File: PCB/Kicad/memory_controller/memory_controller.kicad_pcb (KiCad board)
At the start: 6 copper layers, 0 parts

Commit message: pcb init
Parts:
- added C1: 100nF, Capacitor_SMD:C_0402_1005Metric, F.Cu at (262.9, 150.4)
- added C10: 100nF, Capacitor_SMD:C_0402_1005Metric, F.Cu at (259.7, 170.4)
- added C11: 100nF, Capacitor_SMD:C_0402_1005Metric, F.Cu at (243.1, 152.8)
- added C12: 100nF, Capacitor_SMD:C_0402_1005Metric, F.Cu at (243.1, 140.9)
- added C13: 100nF, Capacitor_SMD:C_0402_1005Metric, F.Cu at (213.7, 132.0)
- added C14: 100nF, Capacitor_SMD:C_0402_1005Metric, F.Cu at (196.7, 132.2)
- added C15: 100nF, Capacitor_SMD:C_0402_1005Metric, F.Cu at (174.9, 100.1)
- added C16: 100nF, Capacitor_SMD:C_0402_1005Metric, F.Cu at (174.6, 83.6)
- added C17: 100nF, Capacitor_SMD:C_0402_1005Metric, F.Cu at (219.2, 83.6)
- added C18: 100nF, Capacitor_SMD:C_0402_1005Metric, F.Cu at (218.9, 100.2)
- added C19: 100nF, Capacitor_SMD:C_0402_1005Metric, F.Cu at (235.8, 106.2)
- added C2: 100nF, Capacitor_SMD:C_0402_1005Metric, F.Cu at (263.0, 167.4)
- added C20: 100nF, Capacitor_SMD:C_0402_1005Metric, F.Cu at (235.8, 119.3)
- added C21: 100nF, Capacitor_SMD:C_0402_1005Metric, F.Cu at (259.9, 120.0)
- added C22: 100nF, Capacitor_SMD:C_0402_1005Metric, F.Cu at (259.9, 106.0)
- added C23: 100nF, Capacitor_SMD:C_0402_1005Metric, F.Cu at (160.3, 87.8)
- added C24: 100nF, Capacitor_SMD:C_0402_1005Metric, F.Cu at (160.4, 126.8)
- added C25: 100nF, Capacitor_SMD:C_0402_1005Metric, F.Cu at (212.4, 150.5)
- added C3: 100nF, Capacitor_SMD:C_0402_1005Metric, F.Cu at (162.9, 181.3)
- added C4: 100nF, Capacitor_SMD:C_0402_1005Metric, F.Cu at (162.7, 164.7)
- added C5: 100nF, Capacitor_SMD:C_0402_1005Metric, F.Cu at (193.7, 164.8)
- added C6: 100nF, Capacitor_SMD:C_0402_1005Metric, F.Cu at (193.5, 181.3)
- added C7: 100nF, Capacitor_SMD:C_0402_1005Metric, F.Cu at (241.6, 170.4)
- added C8: 100nF, Capacitor_SMD:C_0402_1005Metric, F.Cu at (241.6, 184.7)
- added C9: 100nF, Capacitor_SMD:C_0402_1005Metric, F.Cu at (259.7, 184.8)
- added H1: MountingHole_2.2mm_M2_DIN965_Pad, MountingHole:MountingHole_2.2mm_M2_DIN965_Pad, F.Cu at (281.4, 69.6)
- added H2: MountingHole_2.2mm_M2_DIN965_Pad, MountingHole:MountingHole_2.2mm_M2_DIN965_Pad, F.Cu at (281.0, 213.5)
- added H3: MountingHole_2.2mm_M2_DIN965_Pad, MountingHole:MountingHole_2.2mm_M2_DIN965_Pad, F.Cu at (87.5, 212.0)
- added H4: MountingHole_2.2mm_M2_DIN965_Pad, MountingHole:MountingHole_2.2mm_M2_DIN965_Pad, F.Cu at (87.4, 69.6)
- added U1: 74LS245, Package_SO:SOIC-20W_7.5x12.8mm_P1.27mm, F.Cu at (257.5, 142.0)
- added U10: 4b_fulladder__CD74HC283M96, mALUch_lib:CD_SOIC127P600X175-16N, F.Cu at (256.5, 191.9)
- added U11: 74LS377, Package_SO:SSOP-20_5.3x7.2mm_P0.65mm, F.Cu at (239.0, 146.8)
- added U12: 74LS377, Package_SO:SSOP-20_5.3x7.2mm_P0.65mm, F.Cu at (239.0, 158.8)
- added U13: 74LS245, Package_SO:SOIC-20W_7.5x12.8mm_P1.27mm, F.Cu at (205.2, 126.8)
- added U14: 74LS245, Package_SO:SOIC-20W_7.5x12.8mm_P1.27mm, F.Cu at (188.1, 126.9)
- added U15: 74LS245, Package_SO:SOIC-20W_7.5x12.8mm_P1.27mm, F.Cu at (180.2, 92.1)
- added U16: 74LS245, Package_SO:SOIC-20W_7.5x12.8mm_P1.27mm, F.Cu at (180.2, 108.3)
- added U17: 74LS245, Package_SO:SOIC-20W_7.5x12.8mm_P1.27mm, F.Cu at (213.8, 92.1)
- added U18: 74LS245, Package_SO:SOIC-20W_7.5x12.8mm_P1.27mm, F.Cu at (213.8, 108.3)
- added U19: 4xAND__SN74HC08DR, mALUch_lib:SOIC127P600X175-14N, F.Cu at (238.8, 112.8)
- added U2: 74LS245, Package_SO:SOIC-20W_7.5x12.8mm_P1.27mm, F.Cu at (257.5, 159.0)
- added U20: ~, mALUch_lib:SOIC127P600X175-14N, F.Cu at (238.8, 125.8)
- added U21: ~, mALUch_lib:SOIC127P600X175-14N, F.Cu at (257.0, 112.8)
- added U22: 4xAND__SN74HC08DR, mALUch_lib:SOIC127P600X175-14N, F.Cu at (257.0, 127.0)
- added U23: AT28C256-15PU, Package_DIP:DIP-28_W15.24mm_Socket, F.Cu at (141.6, 85.2)
- added U24: AT28C256-15PU, Package_DIP:DIP-28_W15.24mm_Socket, F.Cu at (141.6, 124.2)
- added U25: AS7C1026B-10TCN, Package_SO:TSOP-II-44_10.16x18.41mm_P0.8mm, F.Cu at (204.8, 150.5)
- added U3: 74LS245, Package_SO:SOIC-20W_7.5x12.8mm_P1.27mm, F.Cu at (168.2, 173.2)
- added U4: 74LS245, Package_SO:SOIC-20W_7.5x12.8mm_P1.27mm, F.Cu at (168.3, 189.4)
- added U5: 74LS245, Package_SO:SOIC-20W_7.5x12.8mm_P1.27mm, F.Cu at (188.2, 173.2)
- added U6: 74LS245, Package_SO:SOIC-20W_7.5x12.8mm_P1.27mm, F.Cu at (188.3, 189.4)
- added U7: 4b_fulladder__CD74HC283M96, mALUch_lib:CD_SOIC127P600X175-16N, F.Cu at (238.4, 177.5)
- added U8: 4b_fulladder__CD74HC283M96, mALUch_lib:CD_SOIC127P600X175-16N, F.Cu at (238.4, 191.9)
- added U9: 4b_fulladder__CD74HC283M96, mALUch_lib:CD_SOIC127P600X175-16N, F.Cu at (256.5, 177.5)
- added control1: ~, mALUch_lib:PinHeader_2x10_P2.54mm_Horizontal, F.Cu at (270.5, 116.6)
- added control2: ~, mALUch_lib:PinHeader_2x10_P2.54mm_Horizontal, F.Cu at (270.5, 145.1)
- added gpu1: ~, mALUch_lib:PinHeader_2x10_P2.54mm_Horizontal, F.Cu at (181.2, 203.0)
- added gpu2: ~, mALUch_lib:PinHeader_2x10_P2.54mm_Horizontal, F.Cu at (209.1, 203.0)
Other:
- board outline added: 203.5 x 150.8 mm

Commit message: LEDs + minor fixes
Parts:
- added Dd1: yellow, LED_SMD:LED_0603_1608Metric, F.Cu at (113.5, 92.5)
- added Dd10: yellow, LED_SMD:LED_0603_1608Metric, F.Cu at (114.2, 137.4)
- added Dd11: yellow, LED_SMD:LED_0603_1608Metric, F.Cu at (114.2, 143.0)
- added Dd12: yellow, LED_SMD:LED_0603_1608Metric, F.Cu at (114.2, 148.6)
- added Dd2: yellow, LED_SMD:LED_0603_1608Metric, F.Cu at (113.5, 98.1)
- added Dd3: yellow, LED_SMD:LED_0603_1608Metric, F.Cu at (113.3, 103.7)
- added Dd4: yellow, LED_SMD:LED_0603_1608Metric, F.Cu at (113.5, 109.3)
- added Dd5: yellow, LED_SMD:LED_0603_1608Metric, F.Cu at (113.5, 115.0)
- added Dd6: yellow, LED_SMD:LED_0603_1608Metric, F.Cu at (113.2, 120.6)
- added Dd7: yellow, LED_SMD:LED_0603_1608Metric, F.Cu at (113.5, 126.2)
- added Dd8: yellow, LED_SMD:LED_0603_1608Metric, F.Cu at (113.5, 131.8)
- added Dd9: yellow, LED_SMD:LED_0603_1608Metric, F.Cu at (114.0, 154.2)
- added Dpwr1: green, Diode_SMD:D_0603_1608Metric, F.Cu at (279.2, 181.2)
- added Dr0: red, LED_SMD:LED_0603_1608Metric, F.Cu at (97.8, 87.2)
- added Dr1: red, LED_SMD:LED_0603_1608Metric, F.Cu at (97.7, 92.5)
- added Dr10: red, LED_SMD:LED_0603_1608Metric, F.Cu at (98.4, 139.9)
- added Dr11: red, LED_SMD:LED_0603_1608Metric, F.Cu at (98.7, 145.2)
- added Dr12: red, LED_SMD:LED_0603_1608Metric, F.Cu at (98.5, 150.4)
- added Dr13: red, LED_SMD:LED_0603_1608Metric, F.Cu at (98.7, 155.7)
- added Dr14: red, LED_SMD:LED_0603_1608Metric, F.Cu at (98.7, 161.0)
- added Dr15: red, LED_SMD:LED_0603_1608Metric, F.Cu at (98.7, 166.2)
- added Dr2: red, LED_SMD:LED_0603_1608Metric, F.Cu at (97.7, 97.8)
- added Dr3: red, LED_SMD:LED_0603_1608Metric, F.Cu at (97.7, 103.0)
- added Dr4: red, LED_SMD:LED_0603_1608Metric, F.Cu at (97.8, 108.3)
- added Dr5: red, LED_SMD:LED_0603_1608Metric, F.Cu at (98.0, 113.6)
- added Dr6: red, LED_SMD:LED_0603_1608Metric, F.Cu at (98.0, 118.8)
- added Dr7: red, LED_SMD:LED_0603_1608Metric, F.Cu at (98.0, 124.1)
- added Dr8: red, LED_SMD:LED_0603_1608Metric, F.Cu at (98.0, 129.4)
- added Dr9: red, LED_SMD:LED_0603_1608Metric, F.Cu at (98.0, 134.6)
- added Rd1: 680, Resistor_SMD:R_0402_1005Metric, F.Cu at (110.0, 92.5)
- added Rd10: 680, Resistor_SMD:R_0402_1005Metric, F.Cu at (110.5, 137.4)
- added Rd11: 680, Resistor_SMD:R_0402_1005Metric, F.Cu at (110.5, 143.0)
- added Rd12: 680, Resistor_SMD:R_0402_1005Metric, F.Cu at (110.5, 148.6)
- added Rd2: 680, Resistor_SMD:R_0402_1005Metric, F.Cu at (110.0, 98.1)
- added Rd3: 680, Resistor_SMD:R_0402_1005Metric, F.Cu at (110.0, 103.7)
- added Rd4: 680, Resistor_SMD:R_0402_1005Metric, F.Cu at (110.0, 109.3)
- added Rd5: 680, Resistor_SMD:R_0402_1005Metric, F.Cu at (110.0, 115.0)
- added Rd6: 680, Resistor_SMD:R_0402_1005Metric, F.Cu at (110.0, 120.6)
- added Rd7: 680, Resistor_SMD:R_0402_1005Metric, F.Cu at (110.0, 126.2)
- added Rd8: 680, Resistor_SMD:R_0402_1005Metric, F.Cu at (110.0, 131.8)
- added Rd9: 680, Resistor_SMD:R_0402_1005Metric, F.Cu at (110.0, 154.2)
- added Rgp1: 680, Resistor_SMD:R_0402_1005Metric, F.Cu at (275.5, 181.2)
- added Rr0: 680, Resistor_SMD:R_0402_1005Metric, F.Cu at (94.5, 87.2)
- added Rr1: 680, Resistor_SMD:R_0402_1005Metric, F.Cu at (94.5, 92.5)
- added Rr10: 680, Resistor_SMD:R_0402_1005Metric, F.Cu at (95.0, 139.9)
- added Rr11: 680, Resistor_SMD:R_0402_1005Metric, F.Cu at (95.0, 145.2)
- added Rr12: 680, Resistor_SMD:R_0402_1005Metric, F.Cu at (95.0, 150.4)
- added Rr13: 680, Resistor_SMD:R_0402_1005Metric, F.Cu at (95.0, 155.7)
- added Rr14: 680, Resistor_SMD:R_0402_1005Metric, F.Cu at (95.0, 161.0)
- added Rr15: 680, Resistor_SMD:R_0402_1005Metric, F.Cu at (95.0, 166.2)
- added Rr2: 680, Resistor_SMD:R_0402_1005Metric, F.Cu at (94.5, 97.8)
- added Rr3: 680, Resistor_SMD:R_0402_1005Metric, F.Cu at (94.5, 103.0)
- added Rr4: 680, Resistor_SMD:R_0402_1005Metric, F.Cu at (94.5, 108.3)
- added Rr5: 680, Resistor_SMD:R_0402_1005Metric, F.Cu at (94.5, 113.6)
- added Rr6: 680, Resistor_SMD:R_0402_1005Metric, F.Cu at (94.5, 118.8)
- added Rr7: 680, Resistor_SMD:R_0402_1005Metric, F.Cu at (94.5, 124.1)
- added Rr8: 680, Resistor_SMD:R_0402_1005Metric, F.Cu at (94.5, 129.4)
- added Rr9: 680, Resistor_SMD:R_0402_1005Metric, F.Cu at (94.5, 134.6)
- H1, H2, H3, H4: value MountingHole_2.2mm_M2_DIN965_Pad -> MountingHole_Pad
- moved H2 240.7 mm to (87.2, 70.8)
- moved H3 196.0 mm to (283.5, 213.2)
- moved H4 142.2 mm to (86.8, 211.8)
- moved gpu2 30.9 mm to (178.2, 203.0)
- moved control1 29.3 mm to (271.6, 145.9)
- moved control2 28.1 mm to (271.6, 117.1)
- moved gpu1 25.1 mm to (206.3, 203.0)
- moved H1 0.96 mm to (282.2, 70.0)
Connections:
- net /MODE0 renamed /~{OE}_n
- net /RAM_AS7C1026B/~{OE} renamed /~{OUTPUT_ENABLE}
- net /RAM_AS7C1026B/~{WE} renamed /~{WE}_mem
- net /input_MUX/~{OE}_p renamed /~{OE}_p
- net /input_tri_state_buffer/~{OE} renamed /OUTPUT_ENABLE
- net /memory_logic/WRITE_ENABLE renamed /WRITE_ENABLE
- net /memory_logic/~{OE}_MUX_n renamed /~{OE}_MUX_n
- H1 pad 1: (no net) -> GND
- H2 pad 1: (no net) -> GND
- H3 pad 1: (no net) -> GND
- H4 pad 1: (no net) -> GND

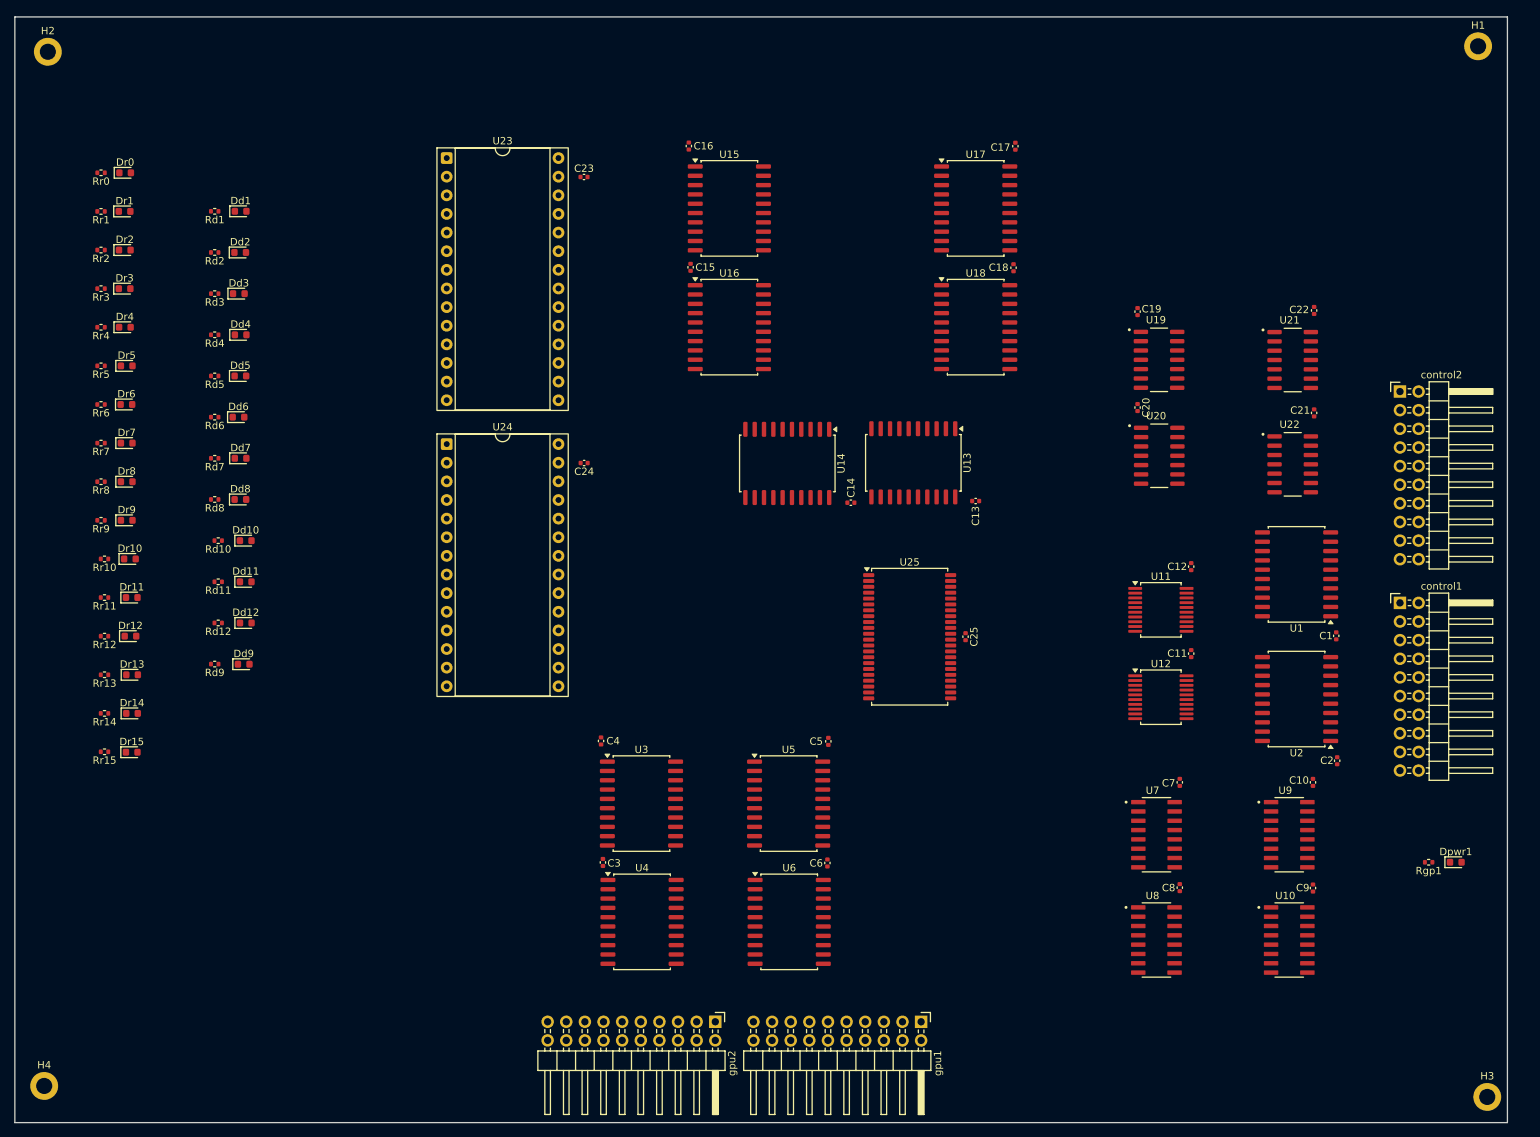
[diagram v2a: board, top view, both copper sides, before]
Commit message: memory controller schematic update
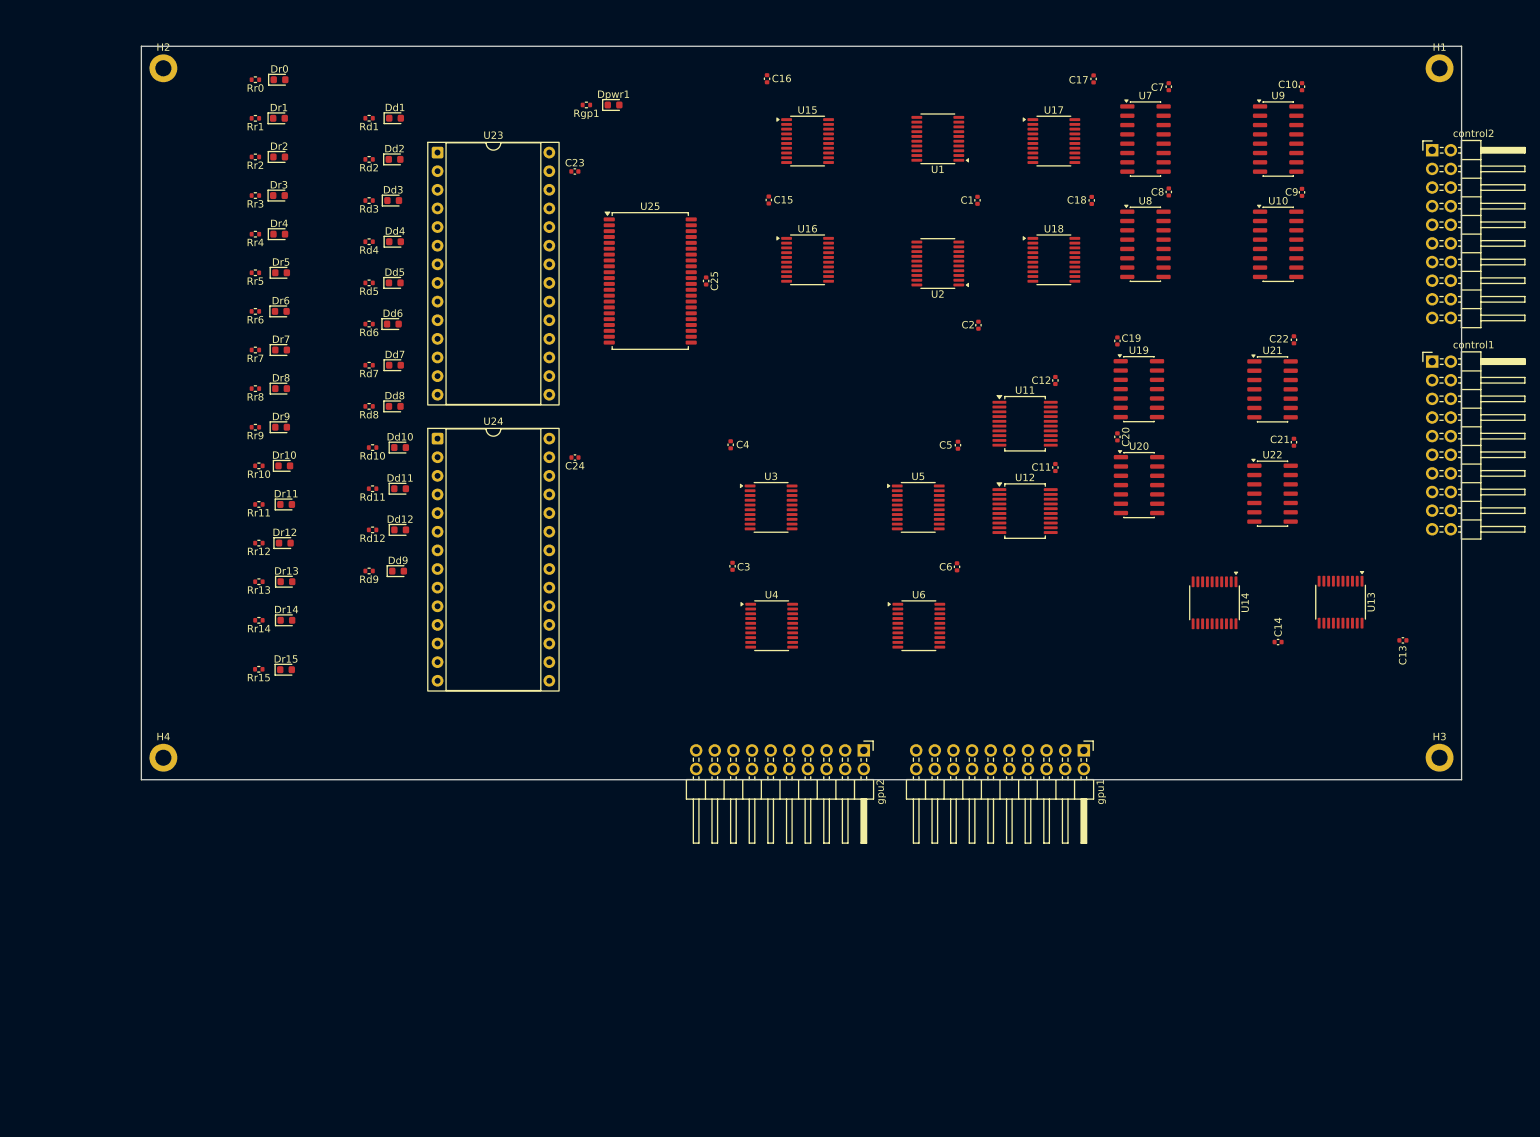
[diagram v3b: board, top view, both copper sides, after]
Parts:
- Dpwr1: footprint Diode_SMD:D_0603_1608Metric -> LED_SMD:LED_0603_1608Metric
- U1, U13, U14, U15, U16, U17, U18, U2, U3, U4, U5, U6: value 74LS245 -> 74245; footprint Package_SO:SOIC-20W_7.5x12.8mm_P1.27mm -> Package_SO:TSSOP-20_4.4x6.5mm_P0.65mm
- U10, U7, U8, U9: value 4b_fulladder__CD74HC283M96 -> 74283; footprint mALUch_lib:CD_SOIC127P600X175-16N -> Package_SO:SOIC-16_3.9x9.9mm_P1.27mm
- U11, U12: value 74LS377 -> 74377
- U19, U22: value 4xAND__SN74HC08DR -> 7408; footprint mALUch_lib:SOIC127P600X175-14N -> Package_SO:SO-14_3.9x8.65mm_P1.27mm
- U20, U21: value ~ -> 7404; footprint mALUch_lib:SOIC127P600X175-14N -> Package_SO:SO-14_3.9x8.65mm_P1.27mm
- control1: value ~ -> out
- gpu1, gpu2: value ~ -> in
- moved Rgp1 154.4 mm to (160.7, 78.0)
- moved Dpwr1 154.4 mm to (164.4, 78.0)
- moved C10 94.9 mm to (258.2, 75.5)
- moved C7 94.9 mm to (240.1, 75.5)
- moved C8 94.9 mm to (240.1, 89.9)
- moved C9 94.9 mm to (258.2, 89.9)
- moved U10 94.9 mm to (255.0, 97.0)
- moved U7 94.9 mm to (236.9, 82.6)
- moved U8 94.9 mm to (236.9, 97.0)
- moved U9 94.9 mm to (255.0, 82.6)
- moved U1 76.9 mm to (208.6, 82.6)
- moved U2 76.9 mm to (208.6, 99.6)
- moved C1 76.9 mm to (214.0, 91.0)
- moved C2 76.9 mm to (214.1, 108.0)
- moved C13 61.3 mm to (272.0, 151.0)
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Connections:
- control1 pad 10: GND -> /MODE2
- control1 pad 8: /MODE2 -> GND
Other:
- board size 203.5 x 150.8 mm -> 180 x 100 mm
